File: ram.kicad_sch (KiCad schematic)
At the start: 59 parts, among them U4 AS6C8008-55ZIN, U5 MT41K512M8DA

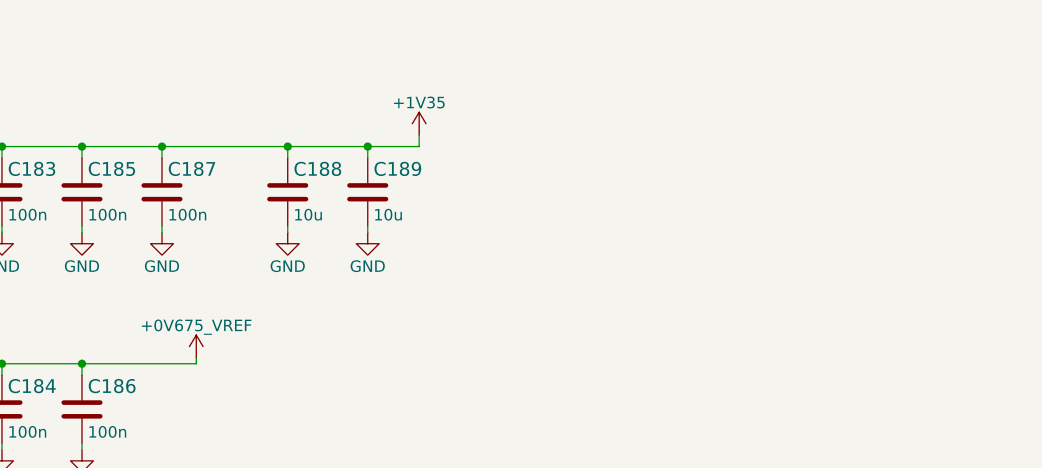
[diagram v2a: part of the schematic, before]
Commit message: Add DDR3L decoupling capacitors
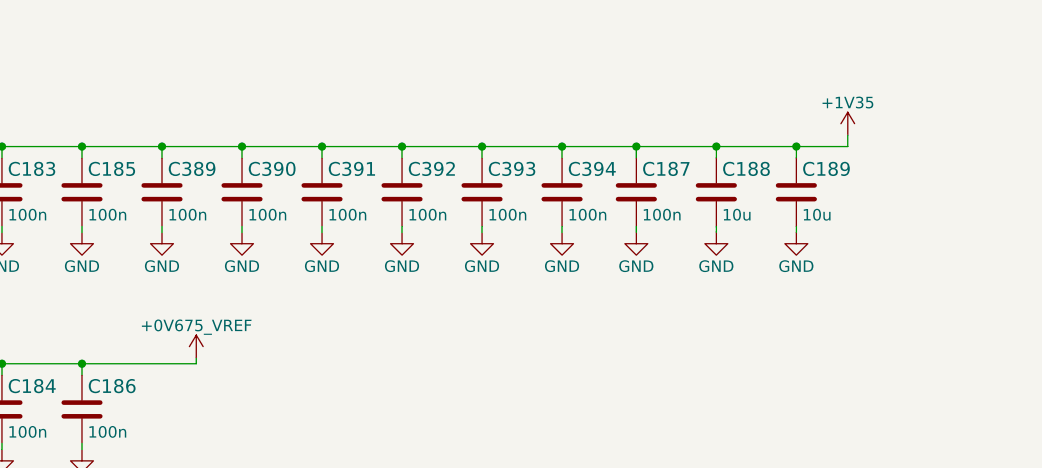
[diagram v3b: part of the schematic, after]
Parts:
- added C389, C390, C391, C392, C393, C394: C_100n_0201, antmicro-footprints:0201-res, symbol antmicroCapacitorsmisc:C_100n_0201
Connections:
- net +1V35: now also C389.1, C390.1, C391.1, C392.1, C393.1, C394.1
- net GND: now also C389.2, C390.2, C391.2, C392.2, C393.2, C394.2
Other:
- moved on the sheet: C187, C188, C189

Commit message: Fix DDR3L placement
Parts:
- removed R12, R13, R14, R15, R16, R17, R18, R19, R20, R21, R22, R23, R24, R25, R26, R27, R28, R29, R30, R31, R33, R41, R42, R44: R_40R2_0201, antmicro-footprints:0201-res, symbol antmicroResistorsmisc:R_40R2_0201
- added R12, R13, R14, R15, R16, R17: 4x39R_0201_array, antmicro-footprints:EXB18V, symbol antmicroResistorNetworksArrays:4x39R_0201_array
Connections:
- net +0V675_VTT: now also R12.5, R12.6, R12.7, R12.8, R13.5, R13.6, R13.7, R13.8, R14.5, R14.6, R14.7, R14.8, R15.5, R15.6, R15.7, R15.8, R16.5, R16.6, R16.7, R16.8, R17.5, R17.6, R17.7, R17.8
- net DDR.A0: now also R14.2
- net DDR.A1: now also R15.4
- net DDR.A10: now also R17.3
- net DDR.A11: now also R16.3
- net DDR.A12: now also R15.2
- net DDR.A13: now also R13.4
- net DDR.A14: now also R16.2
- net DDR.A15: now also R17.2
- net DDR.A2: now also R14.1
- net DDR.A3: now also R12.4
- net DDR.A4: now also R16.1
- net DDR.A5: now also R13.1
- net DDR.A6: now also R17.1
- net DDR.A7: now also R13.2
- net DDR.A8: now also R16.4
- net DDR.A9: now also R13.3
- net DDR.BA0: now also R12.3
- net DDR.BA1: now also R15.3
- net DDR.BA2: now also R14.3
- net DDR.CKE: now also R17.4
- net DDR.ODT: now also R12.1
- net DDR.~{CAS}: now also R15.1
- net DDR.~{CS}: now also R12.2
- net DDR.~{WE}: now also R14.4
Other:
- moved on the sheet: C176, C178, C180, R36, R37, R38, R39, R40, U4

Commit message: Improve RAM sheet
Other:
- moved on the sheet: C166, C167, C168, C169, C170, C171, C172, C173, C174, C175, C176, C177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

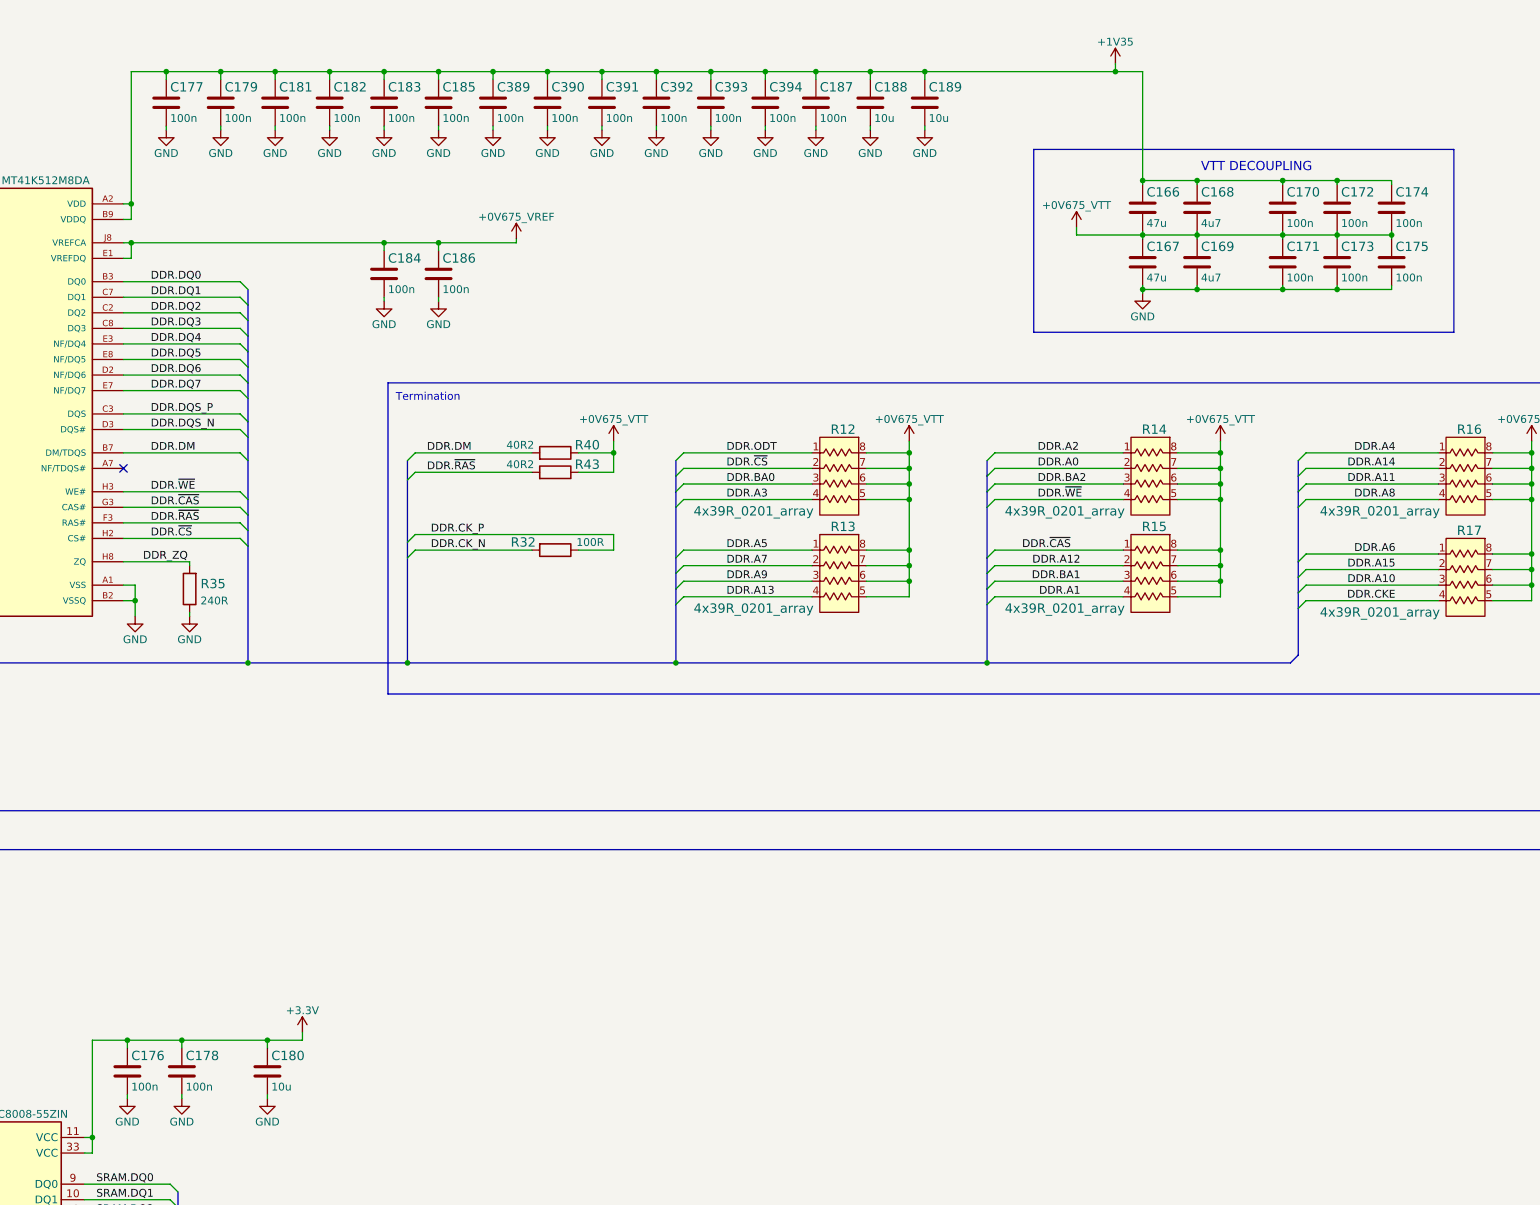
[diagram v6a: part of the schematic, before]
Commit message: Replace 100n to 0402
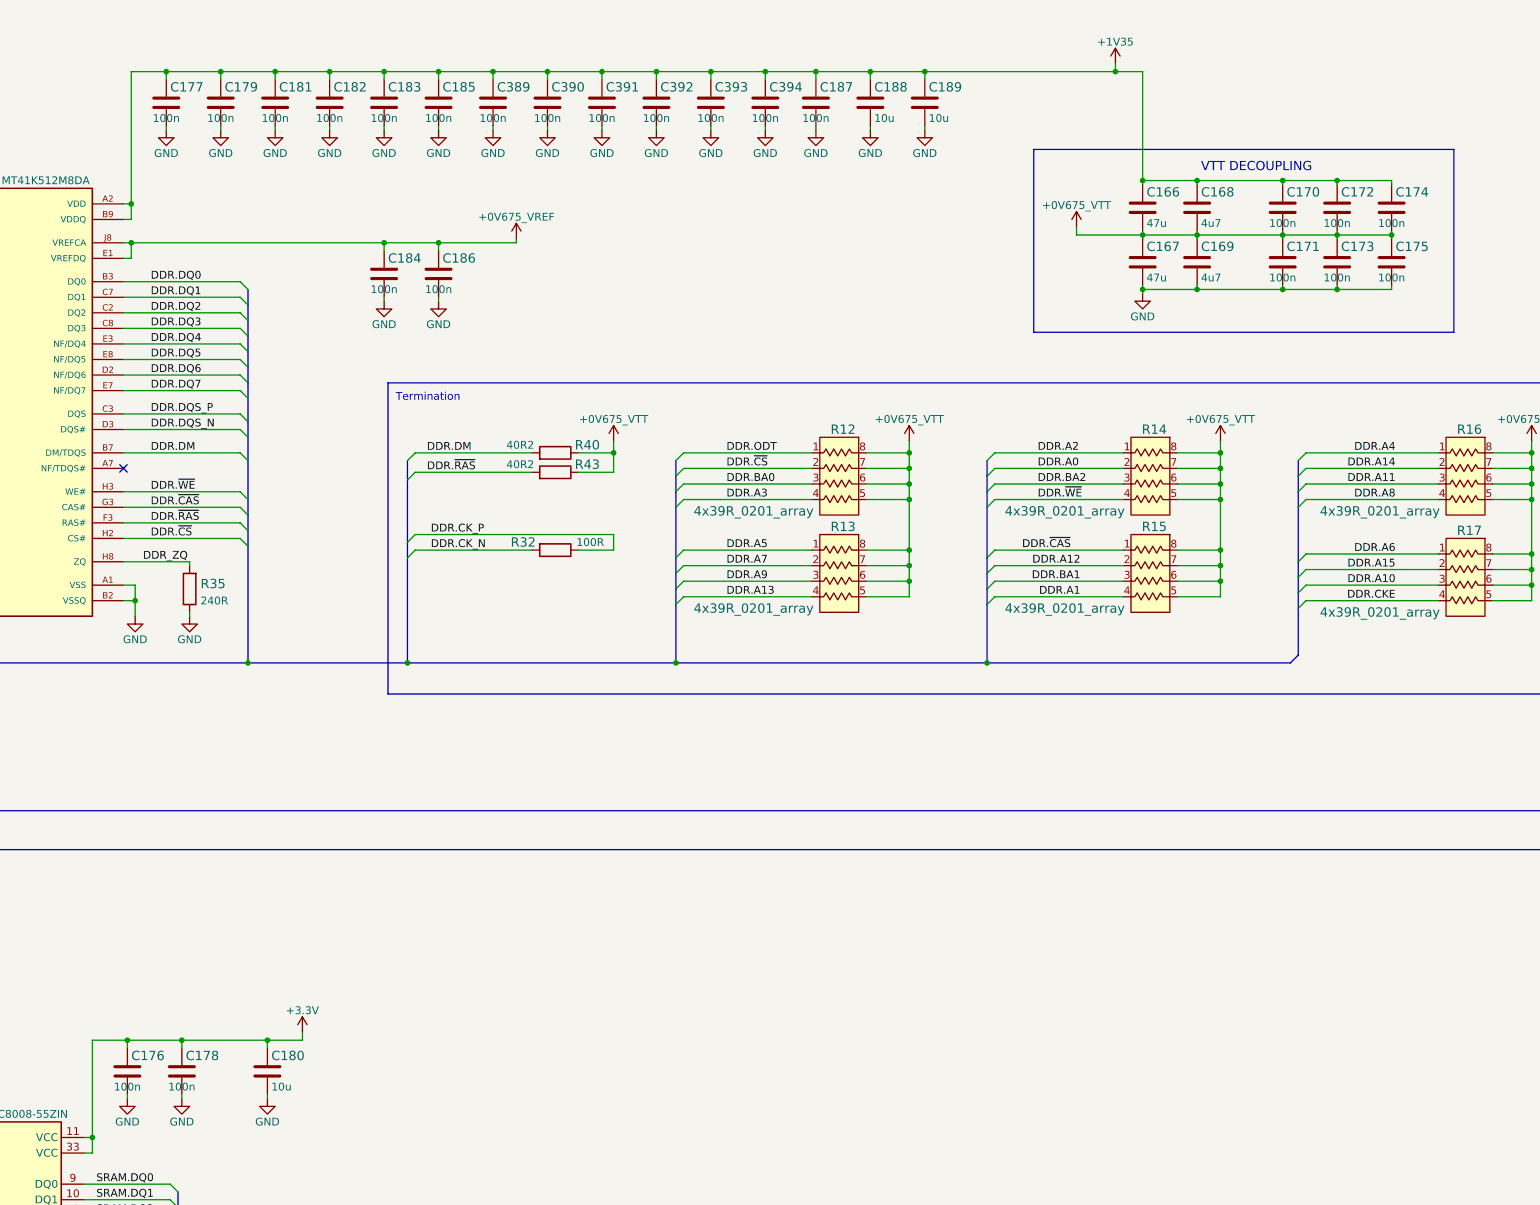
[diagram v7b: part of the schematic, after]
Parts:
- C170, C171, C172, C173, C174, C175, C176, C177, C178, C179, C181, C182, C183, C184, C185, C186, C187, C389, C390, C391, C392, C393, C394: value C_100n_0201 -> C_100n_0402_EIA; footprint antmicro-footprints:0201-res -> antmicro-footprints:0402-cap_EIA; symbol antmicroCapacitorsmisc:C_100n_0201 -> antmicroCapacitors0402:C_100n_0402_EIA; MPN CC0201KRX6S5BB104 -> GRM155R61H104KE14D; Manufacturer YAGEO -> Murata

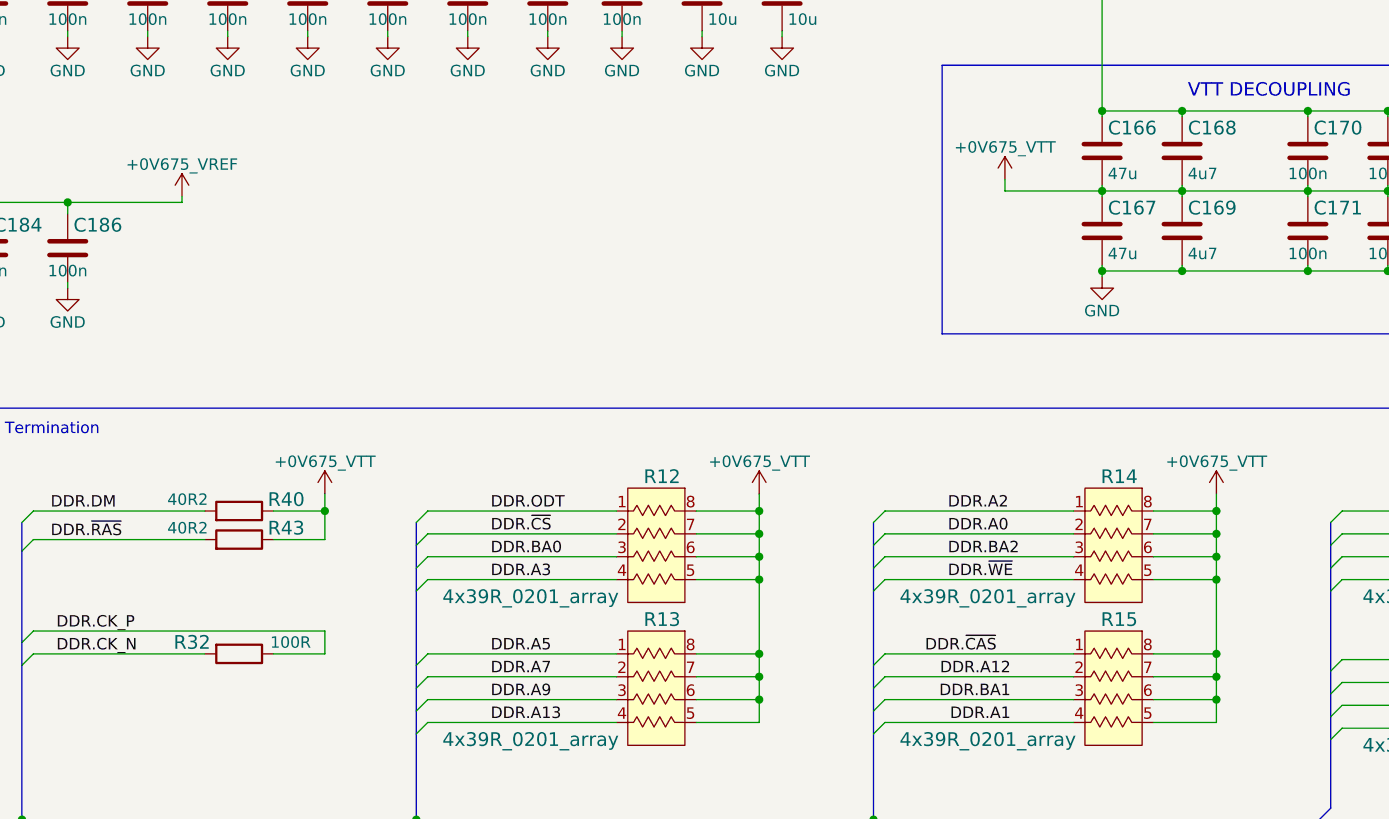
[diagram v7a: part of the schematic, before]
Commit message: Increase 0201 to 0402 components where possible (EIA 0402 footprint)
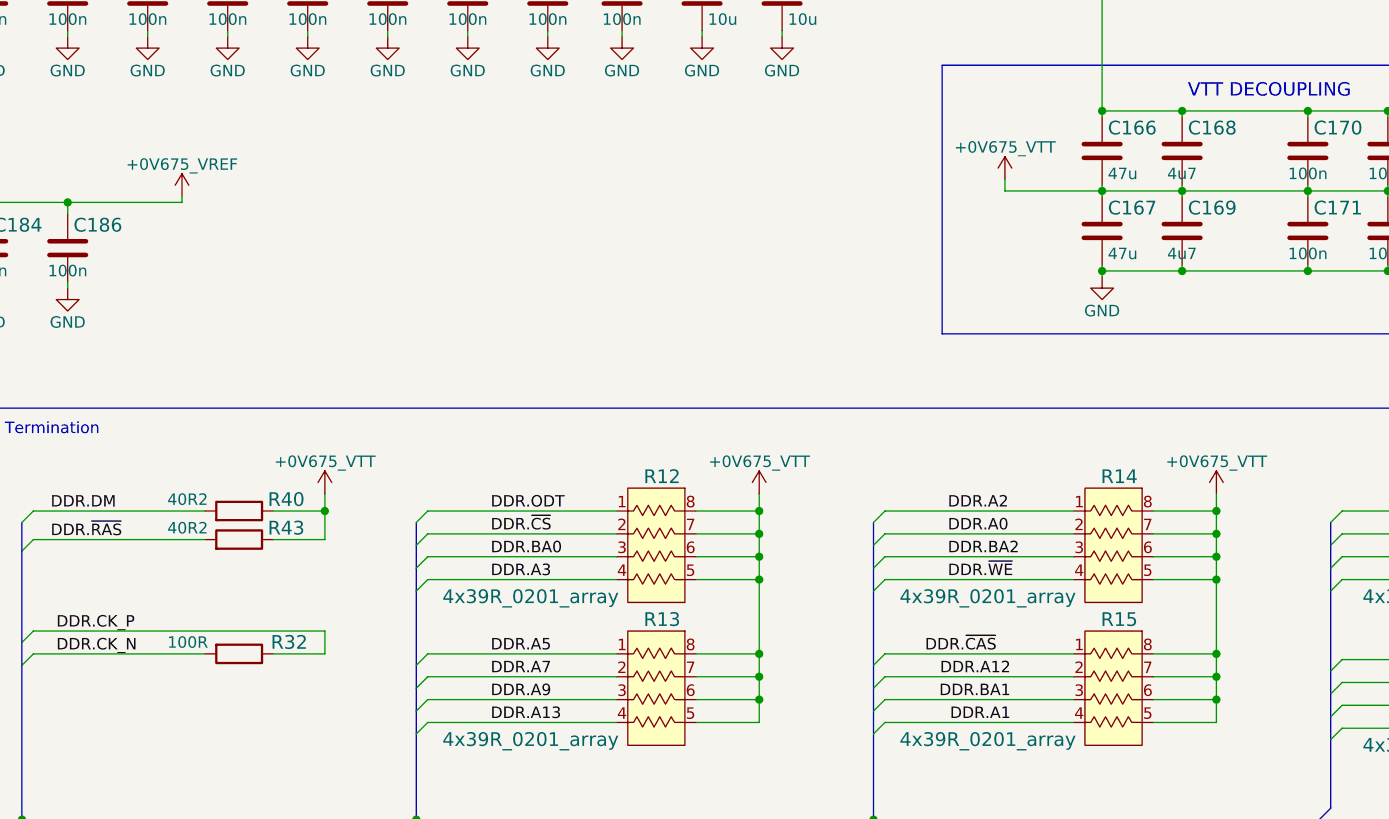
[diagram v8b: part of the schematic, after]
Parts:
- C168, C169: value C_4u7_0402 -> C_4u7_0402_EIA; footprint antmicro-footprints:0402-cap -> antmicro-footprints:0201-cap; symbol antmicroCapacitors0402:C_4u7_0402 -> antmicroCapacitorsmisc:C_4u7_0201; MPN GRM155R61A475MEAAD -> GRM035R60J475ME15D; Manufacturer MURATA -> Murata
- C177, C179, C181, C182, C183, C184, C185, C186, C187, C389, C390, C391, C392, C393, C394: value C_100n_0402_EIA -> C_100n_0201; footprint antmicro-footprints:0402-cap_EIA -> antmicro-footprints:0201-cap; symbol antmicroCapacitors0402:C_100n_0402_EIA -> antmicroCapacitorsmisc:C_100n_0201; MPN GRM155R61H104KE14D -> CC0201KRX6S5BB104; Manufacturer Murata -> YAGEO
- R32: footprint antmicro-footprints:0201-res -> antmicro-footprints:0402-res; symbol antmicroResistorsmisc:R_100R_0201 -> antmicroResistors0402:R_100R_0402; MPN CR0201AFW-1000GAS -> CR0402-FX-1000GLF; Manufacturer Bourns -> BOURNS
